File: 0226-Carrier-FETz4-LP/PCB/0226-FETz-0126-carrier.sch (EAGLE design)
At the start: 3 parts

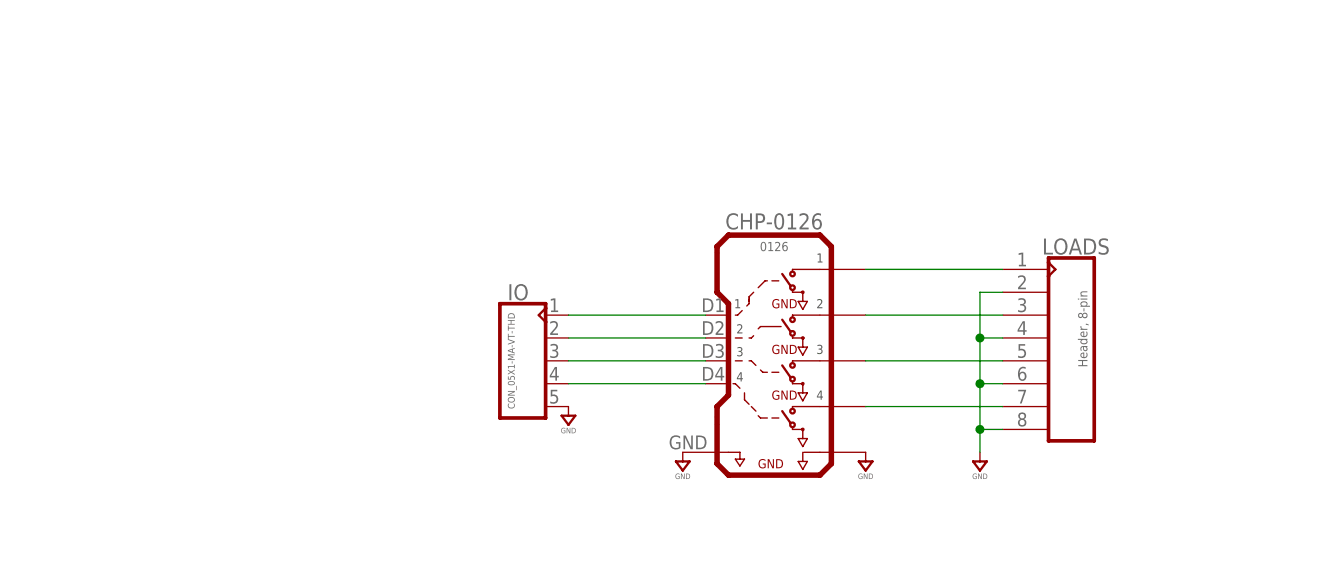
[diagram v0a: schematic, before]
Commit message: Big batch of new PCBs sent to FAB.
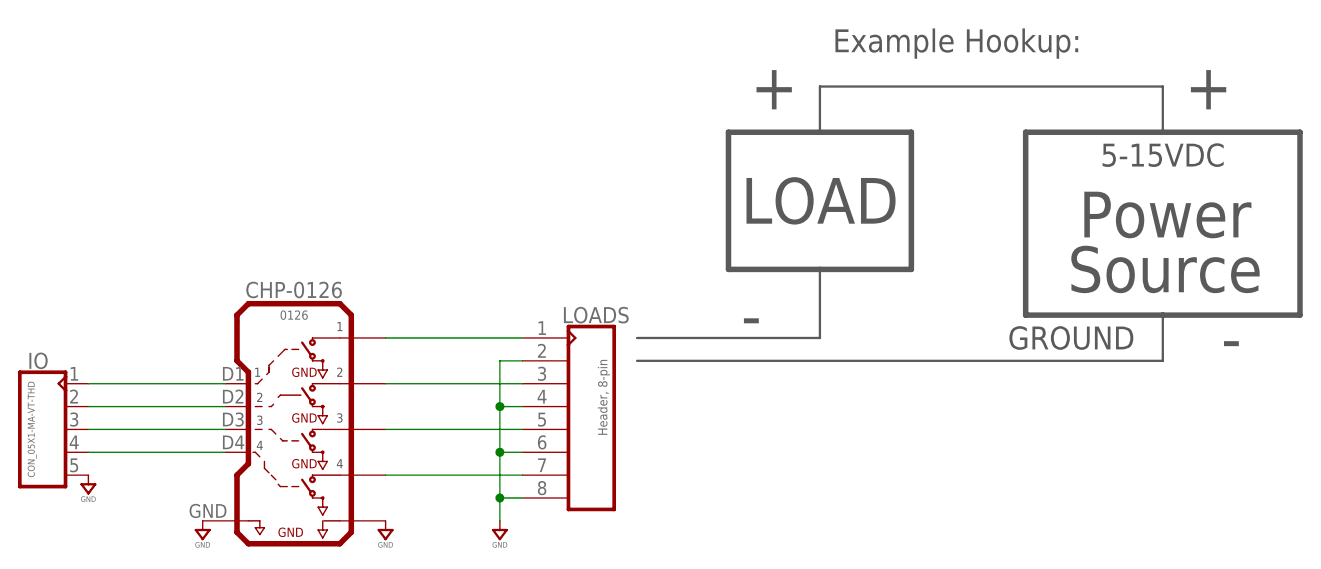
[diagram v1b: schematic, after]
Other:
- note added: "+"
- note added: "-"
- note added: "5-15VDC"
- note added: "Example Hookup:"
- note added: "GROUND"
- note added: "LOAD"
- note added: "Power Source"
- moved on the sheet: CHP-0126, IO, LOADS
